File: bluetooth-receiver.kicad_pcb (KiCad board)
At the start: 2 copper layers, 55.2 x 21.6 mm, 8 parts, among them J1 Barrel_Jack_Switch, J2 AudioJack3_Switch, J3 RCJ-22, U1 m18, U2 dd1718pa

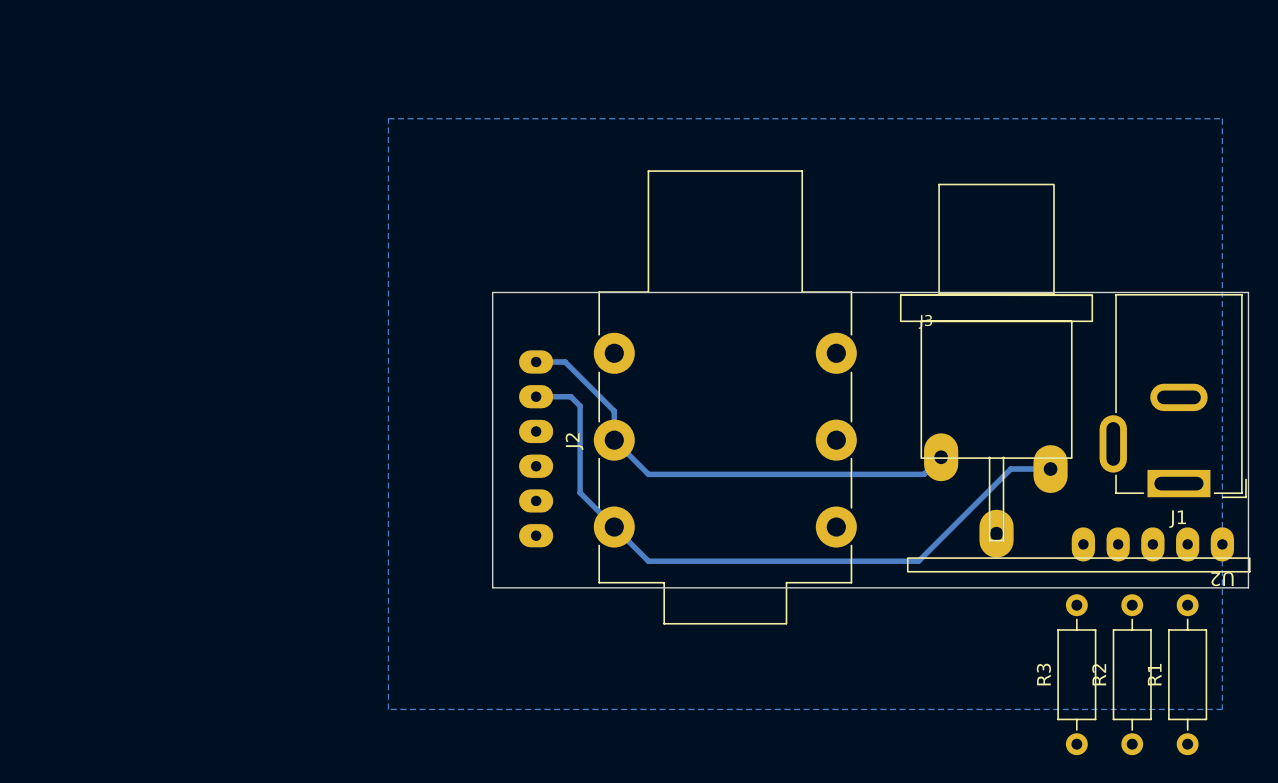
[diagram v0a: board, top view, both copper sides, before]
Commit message: Update bluetooth receiver
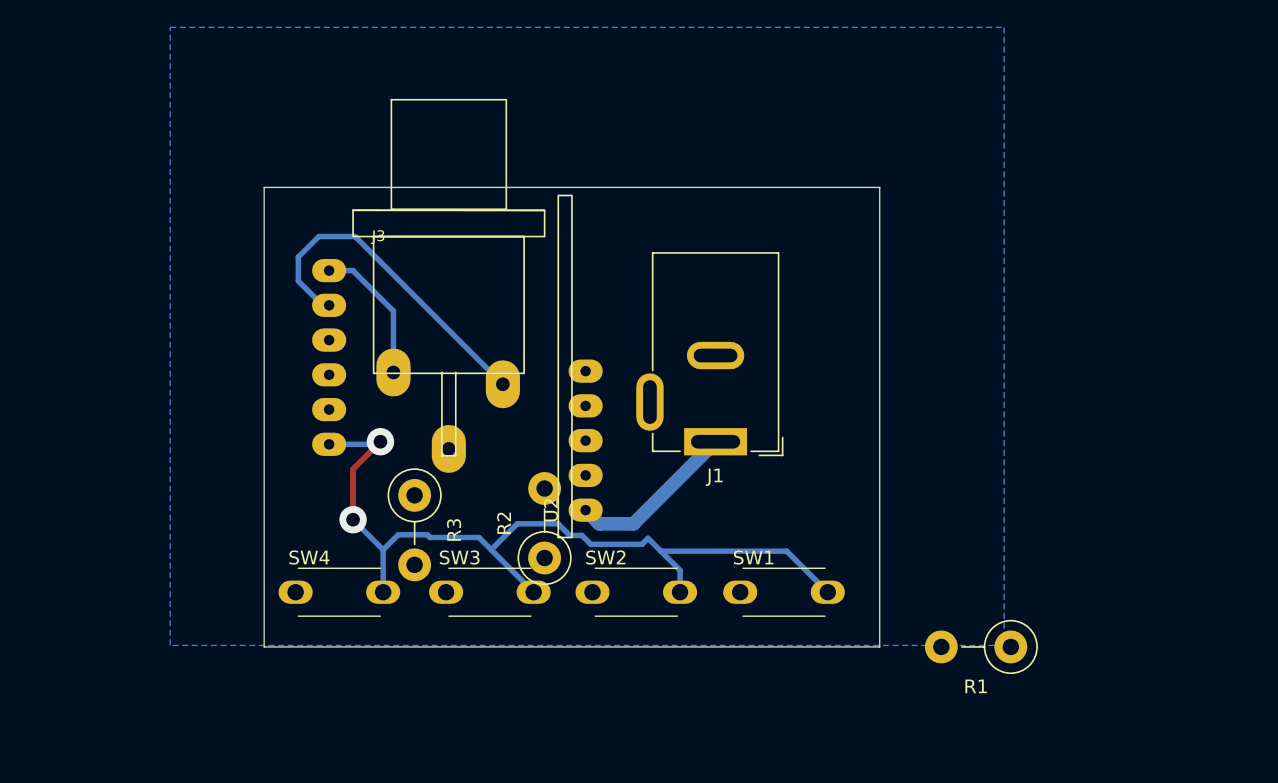
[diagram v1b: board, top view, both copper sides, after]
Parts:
- removed J2: AudioJack3_Switch, Connector_Audio:Jack_6.35mm_Neutrik_NMJ6HFD2-AU_Horizontal
- added SW1: PAUSE, pts636:pts636, F.Cu at (134.3, 107.0)
- added SW2: NEXT, pts636:pts636, F.Cu at (123.5, 107.0)
- added SW3: PREV, pts636:pts636, F.Cu at (112.8, 107.0)
- added SW4: ON_OFF, pts636:pts636, F.Cu at (101.8, 107.0)
- R1, R2, R3: footprint Resistor_THT:R_Axial_DIN0207_L6.3mm_D2.5mm_P10.16mm_Horizontal -> Resistor_THT:R_Axial_DIN0411_L9.9mm_D3.6mm_P5.08mm_Vertical
- moved R3 51.7 mm to (110.5, 99.9), turned to -90 degrees
- moved U2 46.6 mm to (123.0, 101.0), turned to 90 degrees
- moved R2 45.1 mm to (120.0, 104.5)
- moved J3 40.5 mm to (113.0, 91.0)
- moved J1 34.0 mm to (132.5, 96.0)
- moved U1 16.5 mm to (104.2, 89.8)
- moved R1 14.8 mm to (154.1, 111.0), turned to 180 degrees
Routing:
- net Net-(SW1-Pad2): track 0.00 -> 61.2 mm, vias 0 -> 2
- net /R: track 34.8 -> 10.4 mm
- net /L: track 49.1 -> 24.8 mm
- net VBUS: track 0.00 -> 12.4 mm
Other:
- board size 55.2 x 21.6 mm -> 45 x 33.6 mm

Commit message: Prepare for milling
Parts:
- added J2: Power, Connector_PinHeader_2.54mm:PinHeader_1x02_P2.54mm_Vertical, F.Cu at (137.2, 95.6)
- U1: moved to F.Cu
- moved R1 23.5 mm to (132.0, 103.0), turned to 0 degrees
- moved J1 5.00 mm to (133.9, 91.2)
- moved R3 3.97 mm to (113.0, 103.0), turned to 180 degrees
- moved SW1 3.50 mm to (130.8, 107.2)
- moved R2 2.55 mm to (117.9, 103.1)
- moved SW2 2.48 mm to (121.0, 107.2)
- moved SW3 1.56 mm to (111.3, 107.2)
- moved U2 1.00 mm to (124.0, 101.0)
- moved J3 0.79 mm to (113.8, 91.0)
- moved SW4 0.31 mm to (101.5, 107.2)
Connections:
- J1 pad 3: unconnected-(J1-Pad3) -> Net-(J2-Pin_1)
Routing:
- net +5V: track 0.00 -> 26.2 mm
- net GND: track 0.00 -> 21.2 mm
- net Net-(J2-Pin_1): track 0.00 -> 15.2 mm
- net VBUS: track 12.4 -> 22.9 mm
- net Net-(R2-Pad1): track 0.00 -> 5.83 mm
- net Net-(R3-Pad1): track 0.00 -> 4.91 mm
- net /L: track 24.8 -> 19.9 mm
- net Net-(R1-Pad1): track 0.00 -> 4.68 mm
- net /R: track 10.4 -> 7.81 mm
- net Net-(U1-KEY): track 61.2 -> 62.5 mm, vias 2 -> 0
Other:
- board size 45 x 33.6 mm -> 39.8 x 30.3 mm

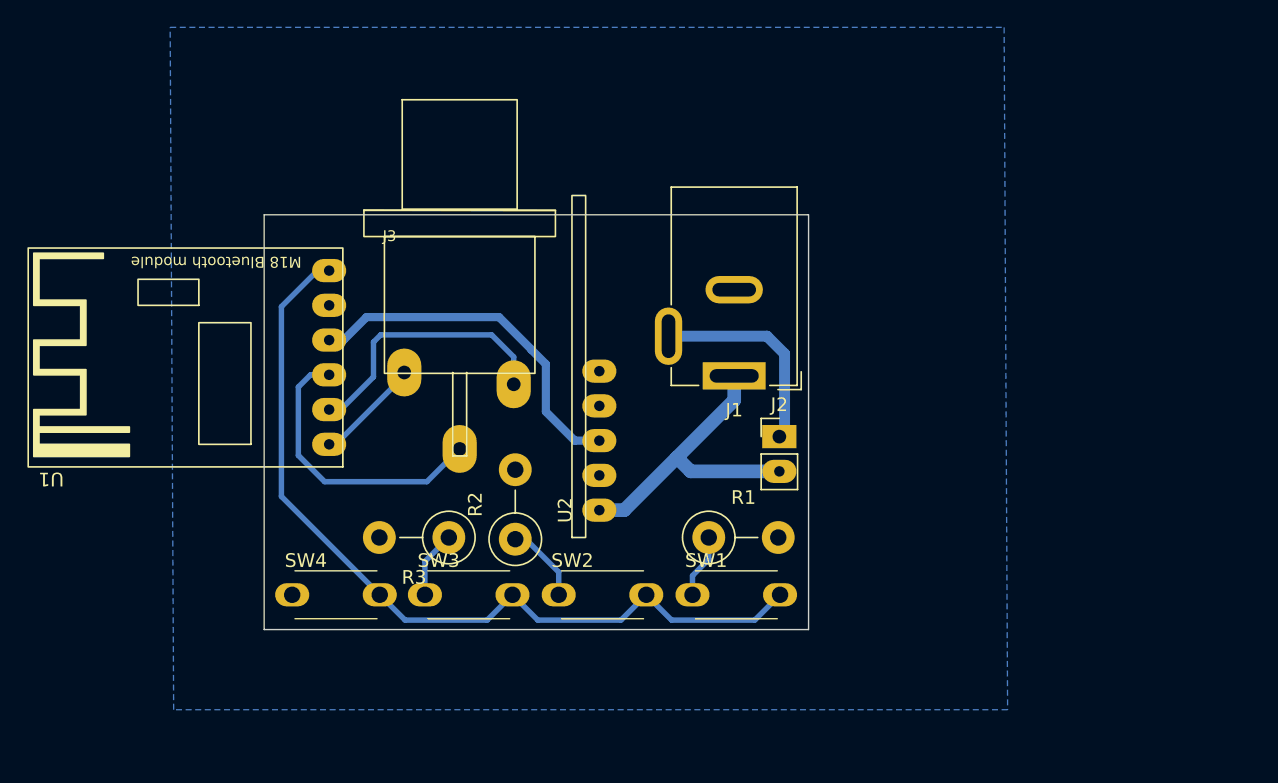
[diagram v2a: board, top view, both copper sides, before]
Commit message: Add mounting holes
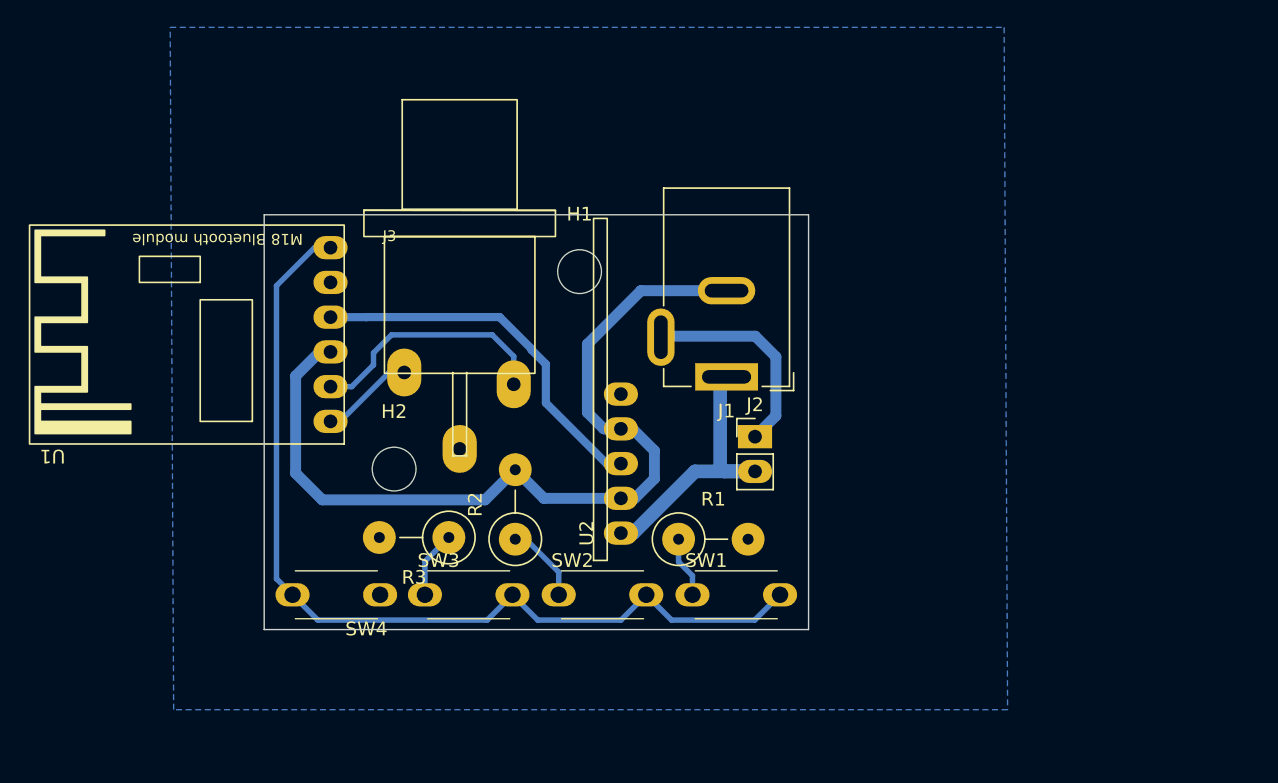
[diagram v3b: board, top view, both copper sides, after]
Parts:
- added H1: MountingHole, MountingHole:MountingHole_3.2mm_M3, F.Cu at (122.6, 83.6)
- added H2: MountingHole, MountingHole:MountingHole_3.2mm_M3, F.Cu at (109.0, 98.0)
- moved SW4 6.42 mm to (108.0, 107.2), turned to 180 degrees
- moved U2 2.30 mm to (125.6, 102.7)
- moved R1 2.21 mm to (129.8, 103.1)
- moved J2 1.78 mm to (135.4, 95.6)
- moved U1 1.68 mm to (104.4, 88.2)
- moved J1 0.56 mm to (133.3, 91.3)
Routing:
- net GND: track 21.2 -> 64.7 mm
- net Net-(U1-KEY): track 62.5 -> 68.4 mm
- net /L: track 19.9 -> 18.2 mm
- net VBUS: track 22.9 -> 21.2 mm
- net +5V: track 26.2 -> 27.4 mm
- net /R: track 7.81 -> 6.87 mm
